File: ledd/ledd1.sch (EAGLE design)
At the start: 8 parts, among them X2 LEDOUT

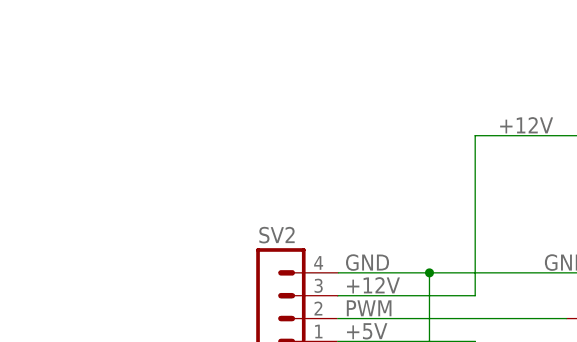
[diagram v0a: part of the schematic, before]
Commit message: ledd: added some TODO comments to ledd1.sch
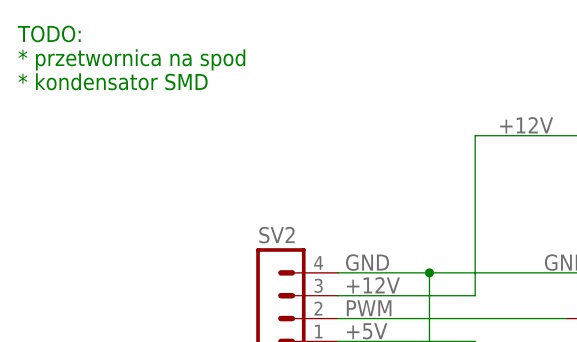
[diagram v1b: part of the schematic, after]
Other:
- note added: "TODO: * przetwornica na spod * kondensator SMD"
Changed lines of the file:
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@@
 <?xml version="1.0" encoding="utf-8"?>
 <!DOCTYPE eagle SYSTEM "eagle.dtd">
-<eagle version="6.4">
+<eagle version="7.1.0">
 <drawing>
 <settings>
@@
 <sheet>
 <plain>
+<text x="147.32" y="198.12" size="1.778" layer="91">TODO:
+* przetwornica na spod
+* kondensator SMD</text>
 </plain>
 <instances>
@@
 </schematic>
 </drawing>
+<compatibility>
+<note version="6.3" minversion="6.2.2" severity="warning">
+Since Version 6.2.2 text objects can contain more than one line,
+which will not be processed correctly with this version.
+</note>
+</compatibility>
 </eagle>
